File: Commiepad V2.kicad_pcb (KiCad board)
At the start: 2 copper layers, 3.8 x 3 mm, 29 parts, among them J1 SSD1306 OLED, SW1 RotaryEncoder_Switch_MP, SW2 SW_Push_45deg, SW3 SW_Push_45deg, SW4 SW_Push_45deg, SW5 SW_Push_45deg, SW6 SW_Push_45deg, SW7 SW_Push_45deg, SW8 SW_Push_45deg, SW9 SW_Push_45deg, U2 XIAO-RP2040-DIP

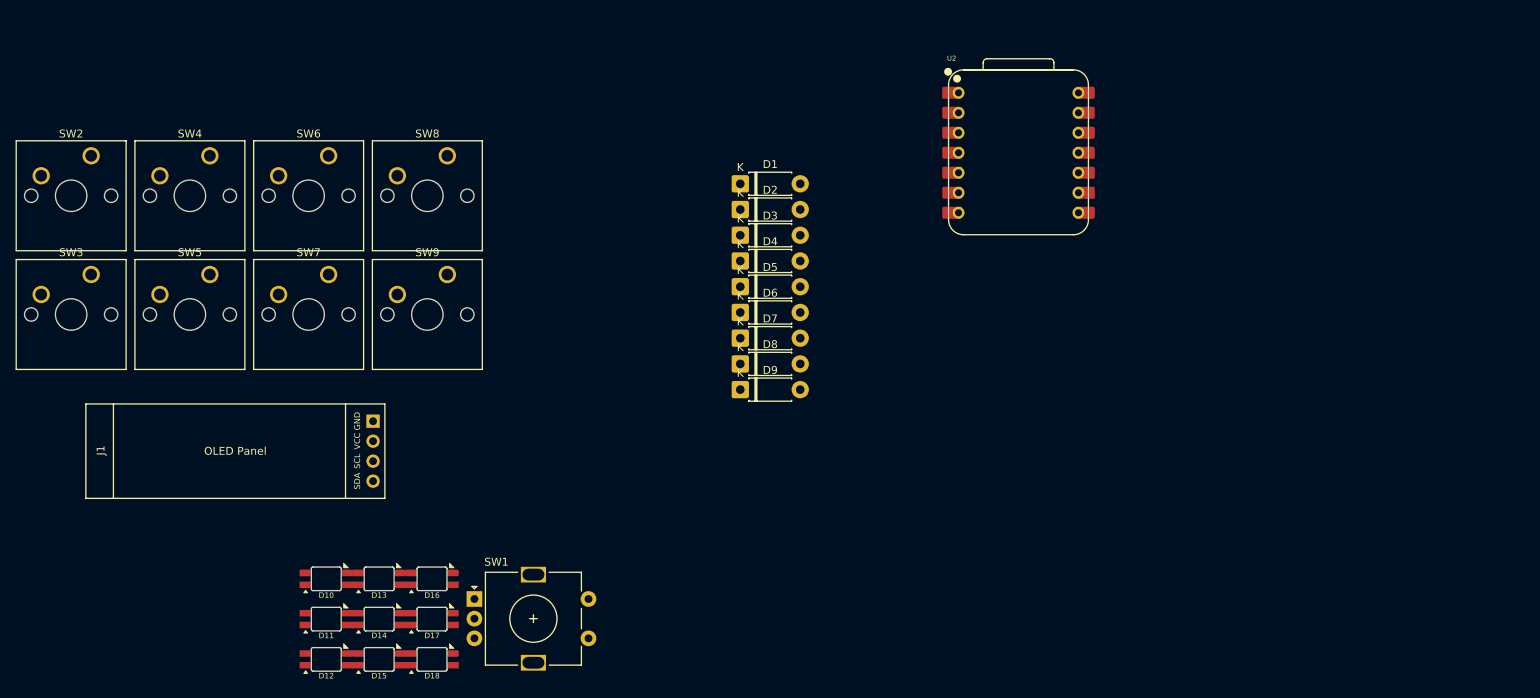
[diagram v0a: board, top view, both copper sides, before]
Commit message: Changed the MCU to nRF52840 for wireless connectivity
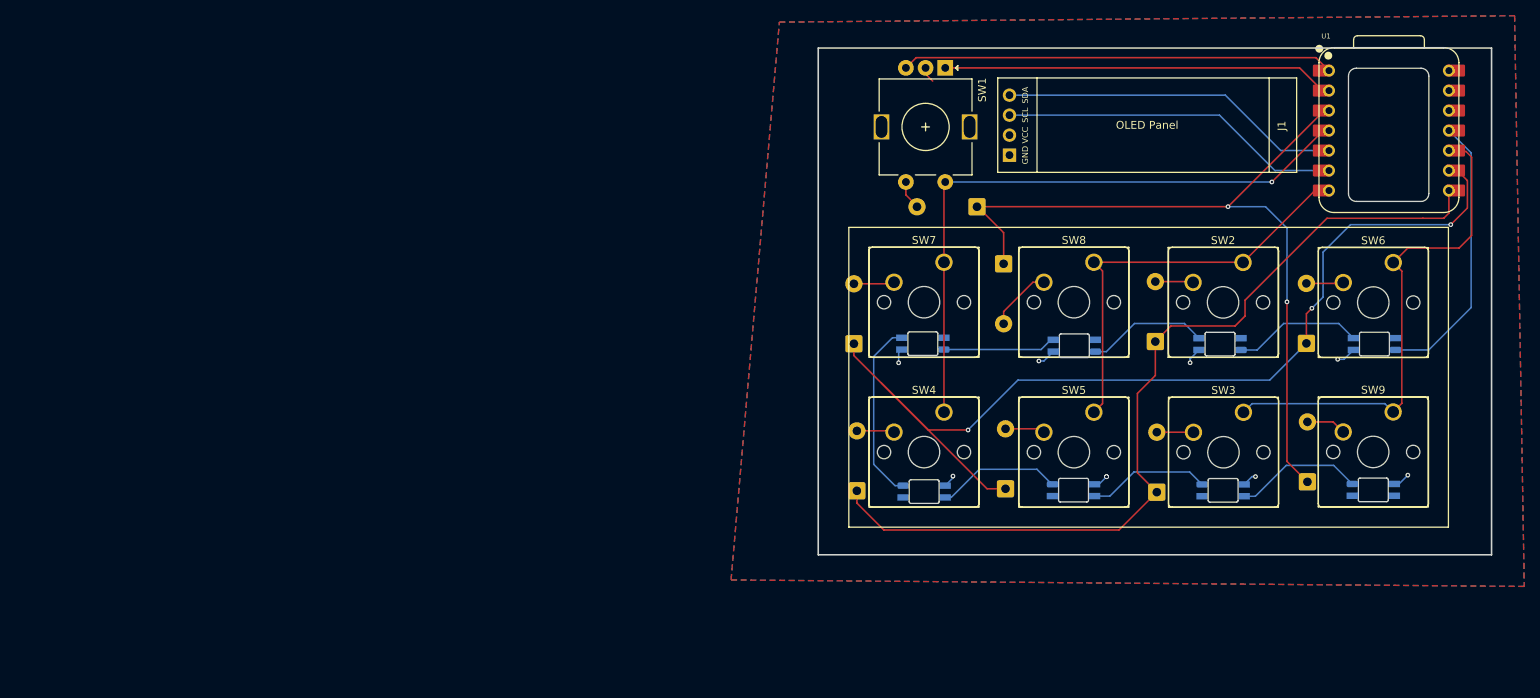
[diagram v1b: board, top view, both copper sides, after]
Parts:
- removed D18: SK6812MINI, FSM8JH:SK6812-MINI-E
- removed U2: XIAO-RP2040-DIP, Seeed Studio XIAO Series Library:XIAO-RP2040-DIP
- added U1: XIAO-nRF52840-DIP, Seeed Studio XIAO Series Library:XIAO-nRF52840-DIP, F.Cu at (196.3, 51.6)
- D1, D10, D11, D12, D13, D14, D15, D16, D17, D2, D3, D4, D5, D6, D7, D8, D9: moved to B.Cu
- moved J1 156.7 mm to (184.5, 56.9), turned to 180 degrees
- moved SW3 147.5 mm to (177.8, 87.4)
- moved SW2 147.0 mm to (177.7, 68.3)
- moved D10 136.5 mm to (194.4, 78.7)
- moved SW6 136.0 mm to (196.8, 68.3)
- moved SW9 121.5 mm to (196.8, 87.3)
- moved D17 120.8 mm to (194.3, 97.2), turned to 180 degrees
- moved D11 118.8 mm to (174.8, 78.7)
- moved SW5 113.7 mm to (158.8, 87.4)
- moved D12 103.1 mm to (156.3, 78.9)
- moved D16 101.2 mm to (175.2, 97.3), turned to 180 degrees
- moved SW4 98.8 mm to (139.7, 87.3)
- moved D15 90.8 mm to (156.2, 97.3), turned to 180 degrees
- moved SW1 90.2 mm to (139.9, 43.6), turned to -90 degrees
- moved SW8 83.3 mm to (158.8, 68.3)
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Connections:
- D10 pad 1: unconnected-(D10-DOUT-Pad1) -> Net-(D10-DOUT)
- D11 pad 1: unconnected-(D11-DOUT-Pad1) -> Net-(D11-DOUT)
- D11 pad 3: unconnected-(D11-DIN-Pad3) -> Net-(D10-DOUT)
- D12 pad 3: unconnected-(D12-DIN-Pad3) -> Net-(D11-DOUT)
- D13 pad 1: unconnected-(D13-DOUT-Pad1) -> Net-(D13-DOUT)
- D14 pad 1: unconnected-(D14-DOUT-Pad1) -> Net-(D14-DOUT)
- D14 pad 3: unconnected-(D14-DIN-Pad3) -> Net-(D13-DOUT)
- D15 pad 3: unconnected-(D15-DIN-Pad3) -> Net-(D14-DOUT)
- D16 pad 1: unconnected-(D16-DOUT-Pad1) -> Net-(D16-DOUT)
- D17 pad 3: unconnected-(D17-DIN-Pad3) -> Net-(D16-DOUT)
- J1 pad 1: SDA -> GND
- J1 pad 2: SCLK -> +5V
- J1 pad 3: +5V -> SCLK
- J1 pad 4: GND -> SDA
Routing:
- net ROW2: track 0.00 -> 128.3 mm, vias 0 -> 3
- net ROW1: track 0.00 -> 112.3 mm
- net ROW3: track 0.00 -> 99.5 mm, vias 0 -> 2
- net COL3: track 0.00 -> 80.9 mm, vias 0 -> 1
- net COL2: track 0.00 -> 64.3 mm
- net Encoder1: track 0.00 -> 55.1 mm
- net COL1: track 0.00 -> 52.8 mm
- net Encoder2: track 0.00 -> 49.3 mm
- net SDA: track 0.00 -> 44.6 mm
- net SCLK: track 0.00 -> 43.5 mm
- net Neopixel: track 0.00 -> 35.7 mm
- net Net-(D13-DOUT): track 0.00 -> 23.1 mm
- net GND: track 0.00 -> 18.4 mm, vias 0 -> 9
- net Net-(D10-DOUT): track 0.00 -> 16.4 mm
- net Net-(D16-DOUT): track 0.00 -> 16.3 mm
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- added copper zone on B.Cu, net +5V
- added copper zone on F.Cu, net GND
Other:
- board size 3.8 x 3 mm -> 85.6 x 64.4 mm

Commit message: Had to re add everything T_T
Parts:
- added G***: LOGO, LOGO, B.Cu at (195.5, 52.5)
- U1: value XIAO-nRF52840-DIP -> XIAO-RP2040-DIP; footprint Seeed Studio XIAO Series Library:XIAO-nRF52840-DIP -> Seeed Studio XIAO Series Library:XIAO-RP2040-DIP
- moved D7 7.01 mm to (150.9, 61.5)
- moved SW1 4.95 mm to (137.3, 47.8)
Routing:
- net +5V: track 0.00 -> 299.3 mm, vias 0 -> 4
- net Net-(D7-A): track 3.76 -> 12.4 mm
- net ROW3: track 99.5 -> 93.1 mm
- net Encoder2: track 49.3 -> 52.7 mm
- net Encoder1: track 55.1 -> 57.8 mm
- net GND: track 18.4 -> 16.3 mm
- net COL3: track 80.9 -> 81.9 mm
- added copper zone on B.Cu, net GND
- removed copper zone on B.Cu, net +5V
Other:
- outline, holes or cut-outs redrawn
- board text added: "Commiepad"
- board text added: "HackClub"
- board text added: "Hasnat4763.me"
- board text added: "Pinnacle of the Soviet Technology"
- board text added: "URAAA!"
